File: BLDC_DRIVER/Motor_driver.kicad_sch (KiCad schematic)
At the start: 58 parts, among them IC1 DRV8303DCAR, Q1 IGP20N65F5, Q2 IGP20N65F5, Q3 IGP20N65F5, Q4 IGP20N65F5, Q5 IGP20N65F5, Q6 IGP20N65F5

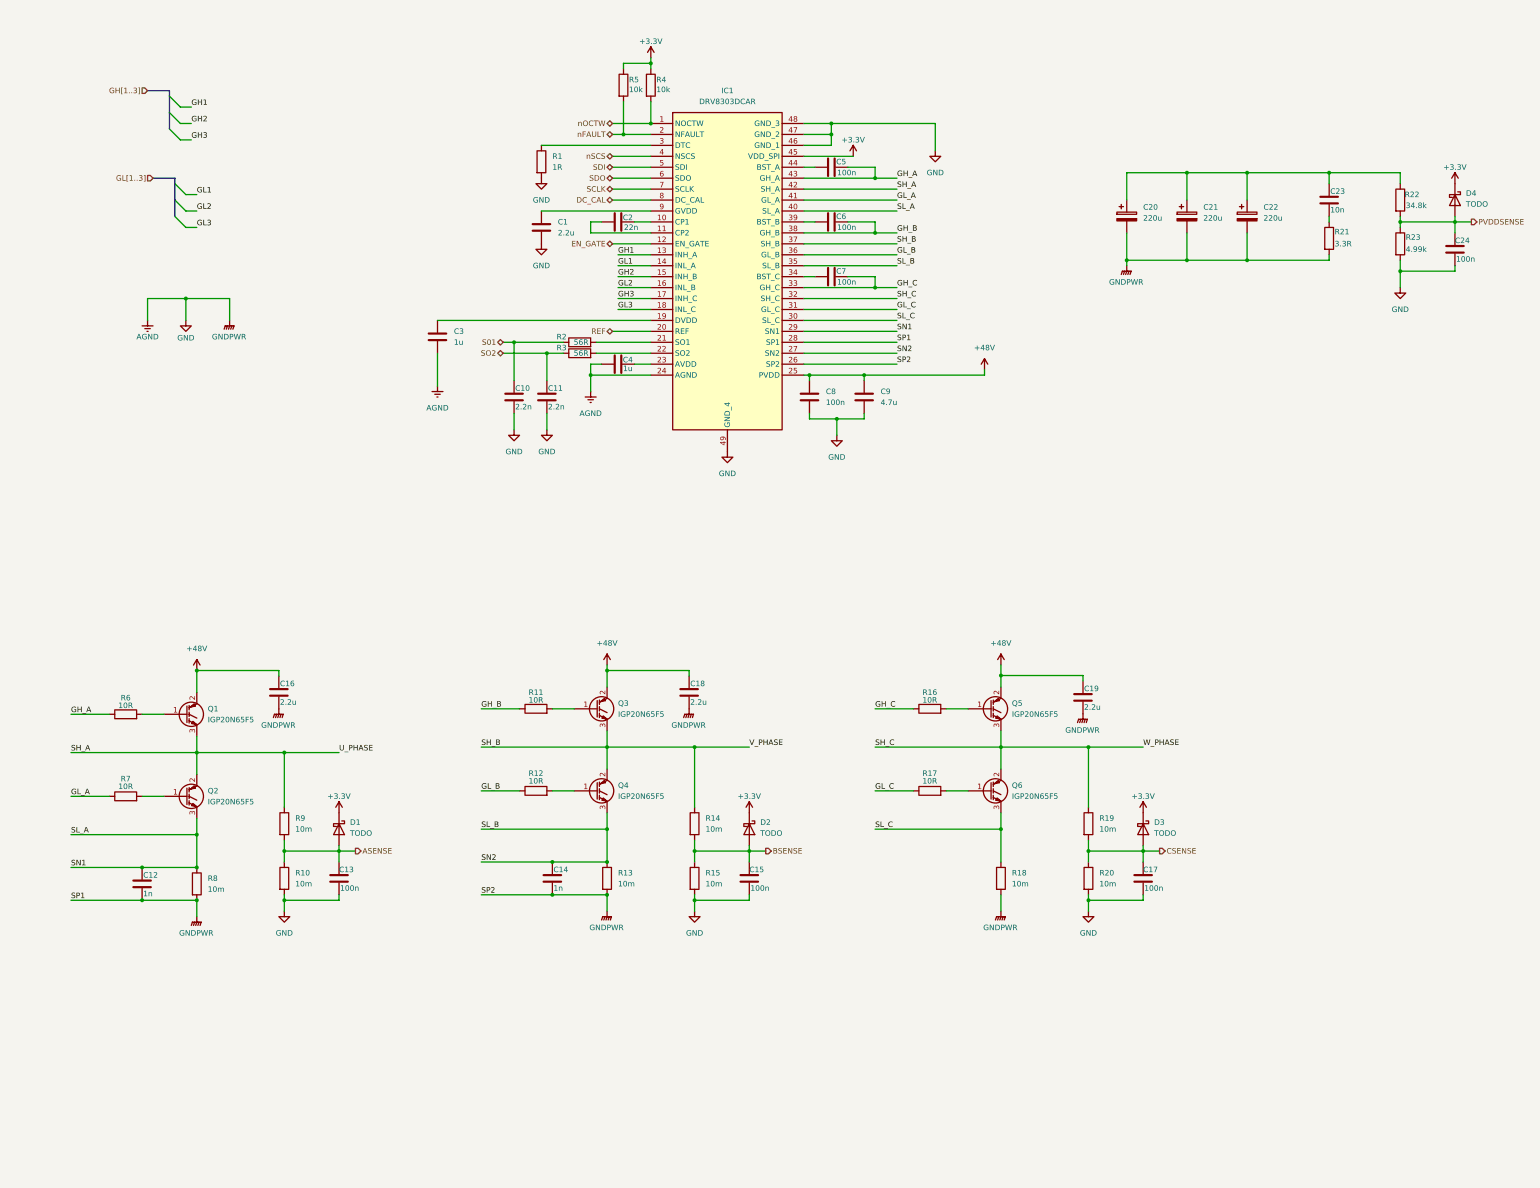
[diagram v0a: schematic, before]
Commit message: BEMF measurement
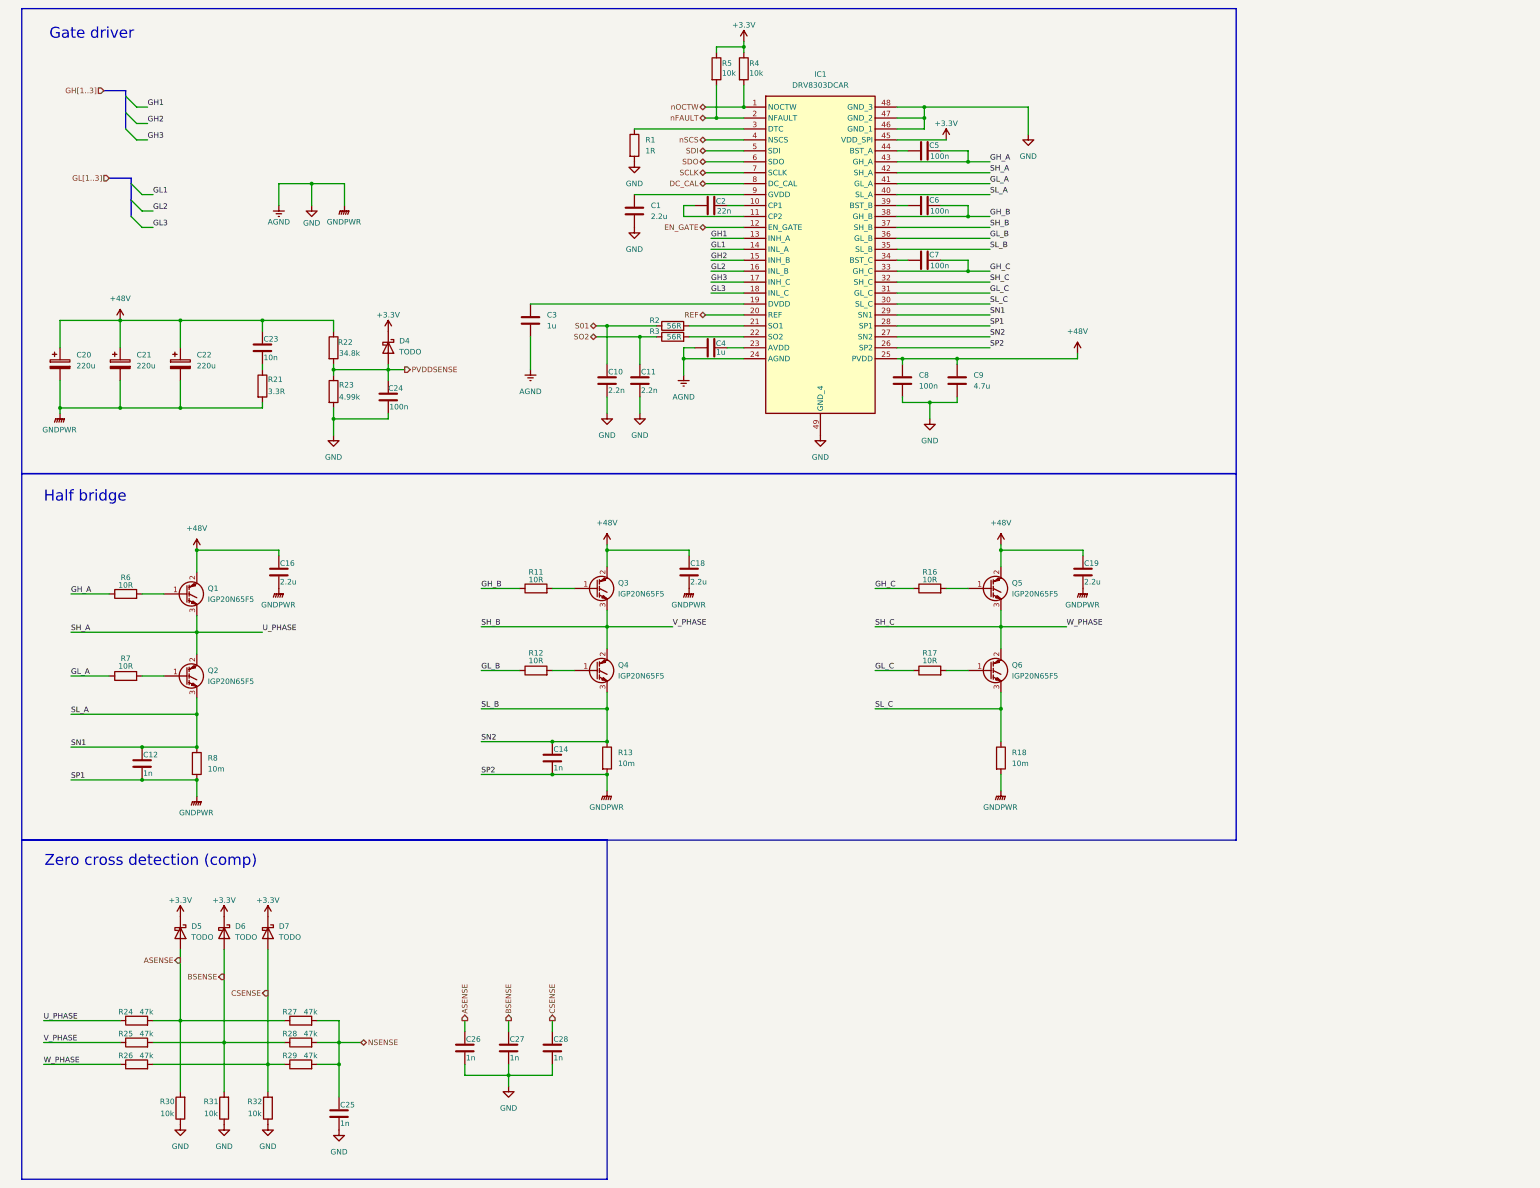
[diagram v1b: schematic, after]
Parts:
- removed C13, C15, C17: 100n, symbol Device:C
- removed D1, D2, D3: TODO, symbol Device:D_Schottky
- removed R10, R14, R15, R19, R20, R9: 10m, symbol Device:R
- added C25, C26, C27, C28: 1n, symbol Device:C
- added D5, D6, D7: TODO, symbol Device:D_Schottky
- added R24, R25, R26, R27, R28, R29: 47k, symbol Device:R
- added R30, R31, R32: 10k, symbol Device:R
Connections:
- net +3.3V: now also D5.1 (K), D6.1 (K), D7.1 (K)
- net +48V: now also C20.1, C21.1, C22.1, C23.1, R22.1
- net AGND: now also C25.2, C26.2, C27.2, C28.2, R30.1, R31.1, R32.1
- net ASENSE: now also C26.1, D5.2 (A), R24.2, R27.1, R30.2
- net BSENSE: now also C27.1, D6.2 (A), R25.2, R28.1, R31.2
- net CSENSE: now also C28.1, D7.2 (A), R26.2, R29.1, R32.2
- net SH_A: now also R24.1
- net SH_B: now also R25.1
- net SH_C: now also R26.1
- new net NSENSE: C25.1, R27.2, R28.2, R29.2
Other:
- note added: "Gate driver"
- note added: "Half bridge"
- note added: "Zero cross detection (comp)"
- moved on the sheet: C1, C10, C11, C12, C14, C16, C18, C19, C2, C20, C21, C22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

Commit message: new driver
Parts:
- removed C1: 2.2u, symbol Device:C
- removed C10, C11: 2.2n, symbol Device:C
- removed C2: 22n, symbol Device:C
- removed C3, C4: 1u, symbol Device:C
- removed C5, C6, C7, C8: 100n, symbol Device:C
- removed C9: 4.7u, symbol Device:C
- removed IC1: DRV8303DCAR, DRV8303DCAR:SOP50P810X120-49N, symbol DRV8303DCAR:DRV8303DCAR
- removed Q1, Q2, Q3, Q4, Q5, Q6: IGP20N65F5, Package_TO_SOT_THT:TO-220-3_Vertical, symbol Device:Q_NIGBT_GCE
- removed R1: 1R, symbol Device:R
- removed R2, R3: 56R, symbol Device:R
- removed R4, R5: 10k, symbol Device:R
- added C13: 47n, symbol Device:C
- added C15: 1n, symbol Device:C
- added C17, C29: 1u, symbol Device:C
- added C30: 100n, symbol Device:C
- added IC2: DRV8323SRTAR, QFN50P600X600X80-41N-D, symbol DRV8323SRTAR:DRV8323SRTAR
- added Q1, Q2, Q3, Q4, Q5, Q6: SQJ170ELP, SQJ160EPT1_GE3, symbol SQJ170ELP-T1_GE3:SQJ170ELP-T1_GE3
- added R33: 0R, symbol Device:R
- added R34, R35: 10k, symbol Device:R
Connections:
- net +3.3V: now also C30.1, IC2.24 (VREF), R33.1, R34.1, R35.1
- net +48V: now also C17.1, IC2.4 (VM), IC2.5 (VDRAIN), Q1.9, Q3.9, Q5.9
- net GH1: now also IC2.34 (INHA)
- net GH2: now also IC2.36 (INHB)
- net GH3: now also IC2.38 (INHC)
- net GL1: now also IC2.35 (INLA)
- net GL2: now also IC2.37 (INLB)
- net GL3: now also IC2.39 (INLC)
- net SCLK: now also IC2.28 (SCLK)
- net SDI: now also IC2.27 (SDI)
- net SDO: now also IC2.26 (SDO), R34.2
- net at R11.2: now also Q3.4
- net at R12.2: now also Q4.4
- net at R16.2: now also Q5.4
- net at R7.2: now also Q2.4
- net at R6.2: now also Q1.4
- net at R17.2: now also Q6.4
- net AGND renamed GND
- net GND: now also C15.2, C29.2, C30.2, IC2.12 (SPB), IC2.19 (SPC), IC2.32 (AGND), IC2.40 (PGND), IC2.41 (EP), IC2.9 (SPA)
- net ASENSE renamed SensVA
- net BSENSE renamed SensVB
- net CSENSE renamed SensVC
- net GH_A renamed GHA
- net GHA: now also IC2.6 (GHA)
- net GH_B renamed GHB
- net GHB: now also IC2.15 (GHB)
- net GH_C renamed GHC
- net GHC: now also IC2.16 (GHC)
- net GL_A renamed GLA
- net GLA: now also IC2.8 (GLA)
- net GL_B renamed GLB
- net GLB: now also IC2.13 (GLB)
- net GL_C renamed GLC
- net GLC: now also IC2.18 (GLC)
- net NSENSE renamed SensVN
- net SH_A renamed SHA
- net SHA: now also IC2.7 (SHA), Q1.1, Q2.9
- net SH_B renamed SHB
- net SHB: now also IC2.14 (SHB), Q3.1, Q4.9
- net SH_C renamed SHC
- net SHC: now also IC2.17 (SHC), Q5.1, Q6.9
- net SL_A renamed SLA
- net SLA: now also IC2.10 (SNA), Q2.1
- net SL_B renamed SLB
- net SLB: now also IC2.11 (SNB), Q4.1
- net SL_C renamed SLC
- net SLC: now also C15.1, IC2.20 (SNC), Q6.1
- new net: C29.1, IC2.33 (DVDD), R33.2
- new net: C13.1, IC2.2 (CPH)
- new net: C13.2, IC2.1 (CPL)
- new net: C17.2, IC2.3 (VCP)
- new net CAL: IC2.31 (CAL)
- new net ENABLE: IC2.30 (ENABLE)
- new net NFAULT: IC2.25 (NFAULT), R35.2
- new net NSCS: IC2.29 (NSCS)
- new net SensIA: IC2.23 (SOA)
- new net SensIB: IC2.22 (SOB)
- new net SensIC: IC2.21 (SOC)
